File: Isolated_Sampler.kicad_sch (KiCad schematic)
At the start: 24 parts, among them U7 AMC1351, U9 TLV6002

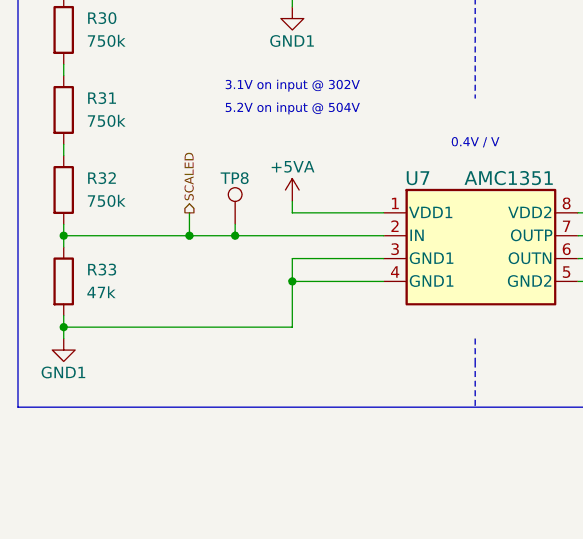
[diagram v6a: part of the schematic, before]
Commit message: *: Add filter capacitors on HV sense inputs
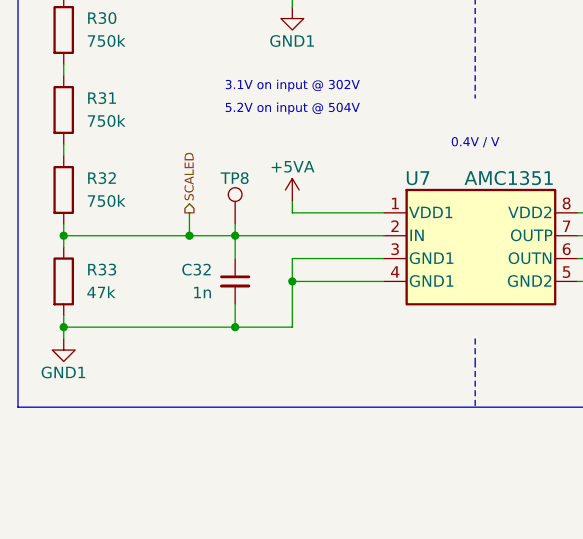
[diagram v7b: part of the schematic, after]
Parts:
- added C32: 1n, Capacitor_SMD:C_0603_1608Metric, symbol Device:C_Small
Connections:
- net GND1: now also C32.2
- net SCALED: now also C32.1
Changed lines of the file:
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@@
+	)
+	(junction
+		(at 58.42 111.76)
+		(diameter 0)
+		(color 0 0 0 0)
 	)
 	(junction
@@
 	(wire
 		(pts
+			(xy 58.42 111.76) (xy 64.77 111.76)
+		)
+		(stroke
+			(width 0)
+			(type default)
+		)
+	)
+	(wire
+		(pts
 			(xy 199.39 125.73) (xy 207.01 125.73)
 		)
@@
 	(wire
 		(pts
+			(xy 58.42 109.22) (xy 58.42 111.76)
+		)
+		(stroke
+			(width 0)
+			(type default)
+		)
+	)
+	(wire
+		(pts
 			(xy 207.01 102.87) (xy 209.55 102.87)
 		)
@@
 	(wire
 		(pts
-			(xy 39.37 111.76) (xy 64.77 111.76)
+			(xy 39.37 111.76) (xy 58.42 111.76)
+		)
+		(stroke
+			(width 0)
+			(type default)
+		)
+	)
+	(wire
+		(pts
+			(xy 58.42 101.6) (xy 58.42 104.14)
 		)
 		(stroke
@@
 					(unit 1)
 				)
+			)
+		)
+	)
+	(symbol
+		(lib_id "Device:C_Small")
+		(at 58.42 106.68 0)
+		(unit 1)
+		(exclude_from_sim no)
+		(in_bom yes)
+		(on_board yes)
+		(dnp no)
+		(property "Reference" "C32"
+			(at 55.88 105.4162 0)
+			(effects
+				(font
+					(size 1.27 1.27)
+				)
+				(justify right)
+			)
+		)
+		(property "Value" "1n"
+			(at 55.88 107.9562 0)
+			(effects
+				(font
+					(size 1.27 1.27)
+				)
+				(justify right)
+			)
+		)
+		(property "Footprint" "Capacitor_SMD:C_0603_1608Metric"
+			(at 58.42 106.68 0)
+			(effects
+				(font
+					(size 1.27 1.27)
+				)
+				(hide yes)
+			)
+		)
+		(property "Datasheet" "~"
+			(at 58.42 106.68 0)
+			(effects
+				(font
+					(size 1.27 1.27)
+				)
+				(hide yes)
+			)
+		)
+		(property "Description" "Unpolarized capacitor, small symbol"
+			(at 58.42 106.68 0)
+			(effects
+				(font
+					(size 1.27 1.27)
+				)
+				(hide yes)
+			)
+		)
+		(pin "2"
+		)
+		(pin "1"
+		)
+		(instances
+			(project ""
+				(path "/c467677d-b98c-4488-bd11-965ef67263b2/5111e28e-8231-41c0-b506-a567affaf28a/40675a50-a5c6-4759-acd6-914b3ce60c39"
+					(reference "C32")
+					(unit 1)
+				)
+				(path "/c467677d-b98c-4488-bd11-965ef67263b2/5111e28e-8231-41c0-b506-a567affaf28a/481c6b85-c613-4759-b3cf-851f0c736d9a"
+					(reference "C33")
+					(unit 1)
+				)

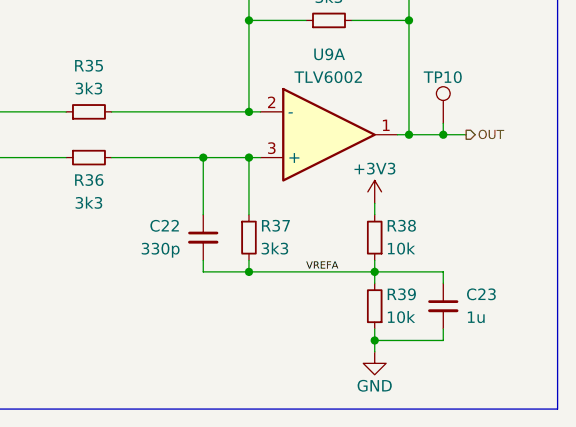
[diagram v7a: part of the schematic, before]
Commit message: *: Change single-ended conversion bias resistors from 10k to 1k
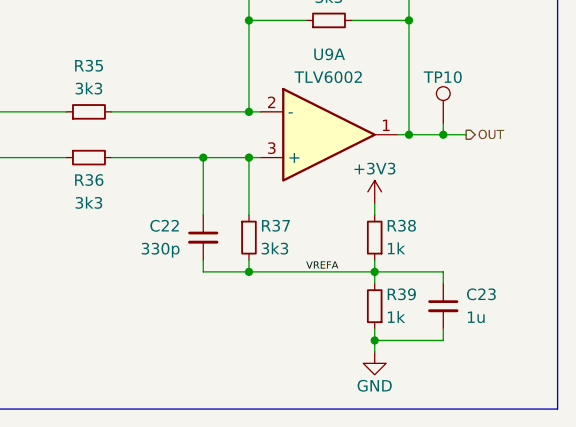
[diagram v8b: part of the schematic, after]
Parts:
- R38, R39: value 10k -> 1k; Dist # C25804 -> C21190; Mfr # 0603WAF1002T5E -> 0603WAF1001T5E
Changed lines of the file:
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@@
 			)
 		)
-		(property "Value" "10k"
+		(property "Value" "1k"
 			(at 200.66 115.57 0)
 			(effects
@@
 			)
 		)
-		(property "Dist #" "C25804"
+		(property "Dist #" "C21190"
 			(at 199.39 114.3 0)
 			(effects
@@
 			)
 		)
-		(property "Mfr #" "0603WAF1002T5E"
+		(property "Mfr #" "0603WAF1001T5E"
 			(at 199.39 114.3 0)
 			(effects
@@
 			)
 		)
-		(property "Value" "10k"
+		(property "Value" "1k"
 			(at 200.66 123.19 0)
 			(effects
@@
 			)
 		)
-		(property "Dist #" "C25804"
+		(property "Dist #" "C21190"
 			(at 199.39 121.92 0)
 			(effects
@@
 			)
 		)
-		(property "Mfr #" "0603WAF1002T5E"
+		(property "Mfr #" "0603WAF1001T5E"
 			(at 199.39 121.92 0)
 			(effects
